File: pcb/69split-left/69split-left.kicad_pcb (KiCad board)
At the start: 2 copper layers, 157.1 x 105.3 mm, 89 parts, among them J1 Conn_02x03_Odd_Even, J2 USB_C_Receptacle, J3 USB_C_Receptacle_USB2.0_14P, SW1 SW_Push, SW10 Q, SW11 W, SW12 E, SW13 R, SW14 T, SW15 Caps Lock, SW16 A, SW17 S, SW18 D, SW19 F, SW2 Esc, SW20 G, SW21 Shift, SW22 \|, SW23 Z, SW24 X, SW25 C, SW26 V, SW27 B, SW28 Ctrl, SW29 Win, SW3 !,1,,F1, SW30 Alt, SW31 Space, SW4 @,2,,F2, SW5 #,3,,F3, SW6 $,4,,F4, SW7 %,5,,F5, SW8 ^,6,,F6, SW9 Tab, U1 ATmega32U4-AU, U2 TLV76133DCY, Y1 Crystal

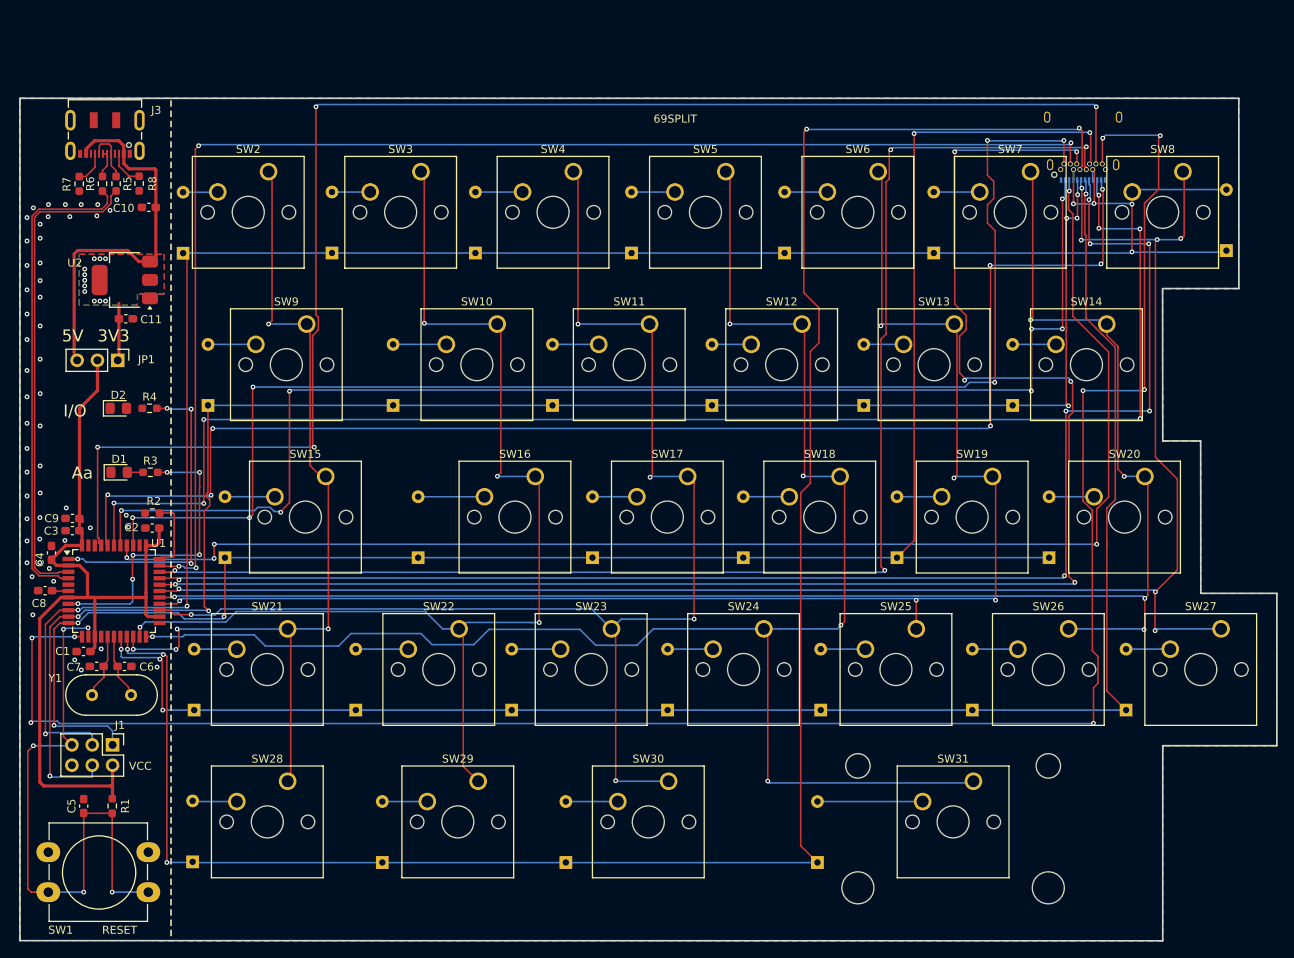
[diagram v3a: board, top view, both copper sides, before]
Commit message: Started changing things gain to use an I/O expander with I2C.
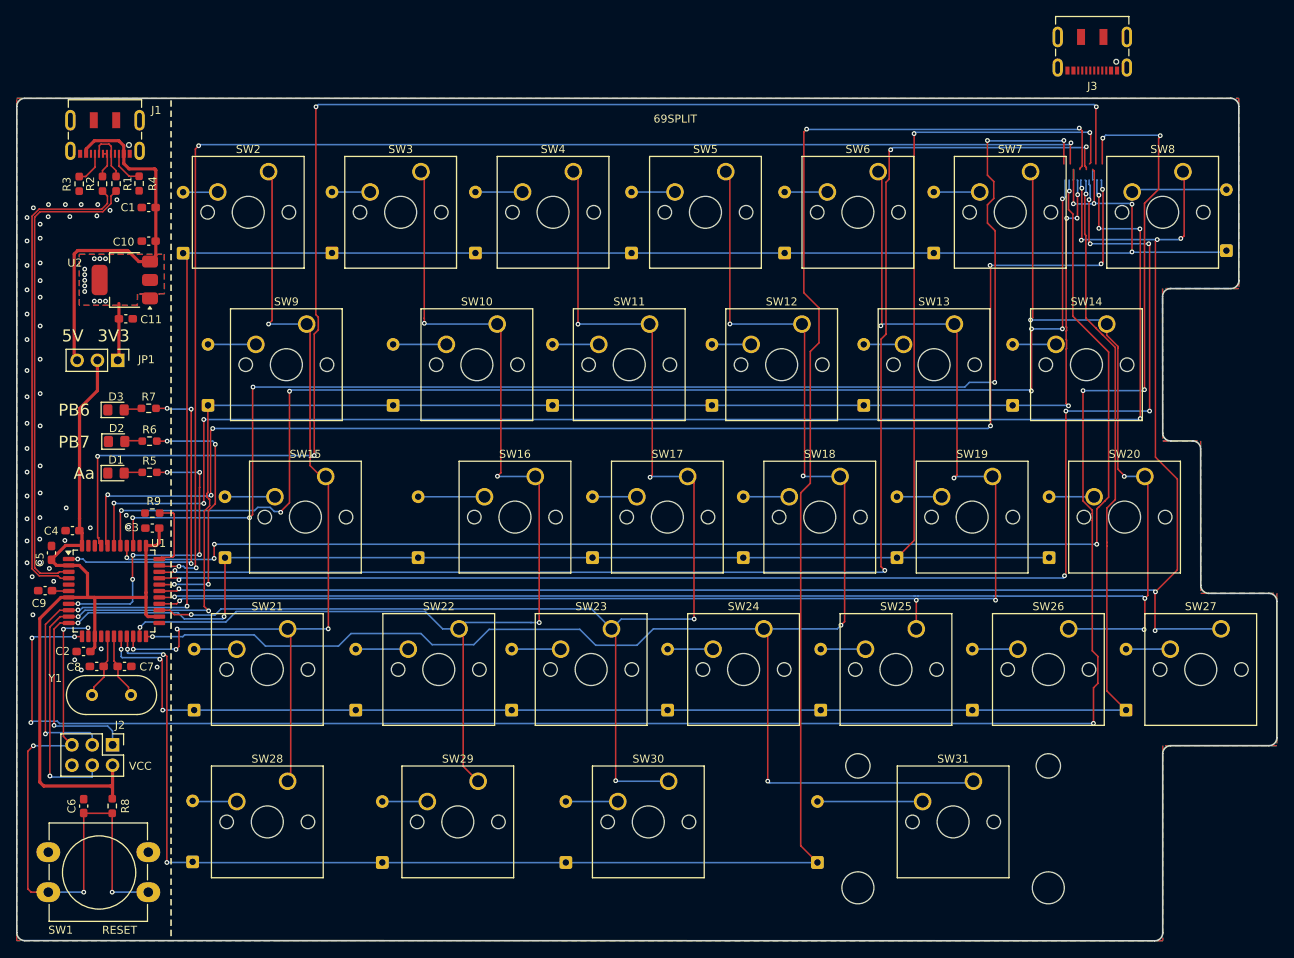
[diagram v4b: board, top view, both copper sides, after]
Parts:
- removed the J2 at (192.9, 43.0)
- added D3: Red LED, LED_SMD:LED_0805_2012Metric_Pad1.15x1.40mm_HandSolder, F.Cu at (72.0, 76.8)
- added J3: USB_C_Receptacle_USB2.0_16P, Connector_USB:USB_C_Receptacle_JAE_DX07S016JA1R1500, F.Cu at (194.0, 31.3)
- added R7: 200R, Resistor_SMD:R_0603_1608Metric_Pad0.98x0.95mm_HandSolder, F.Cu at (76.1, 76.6)
- J1: renamed from J3; value USB_C_Receptacle_USB2.0_14P -> USB_C_Receptacle_USB2.0_16P
- SW4: value @,2,,F2 -> ",2,,F2
- SW5: value #,3,,F3 -> £,3,,F3
- moved C1 40.0 mm to (76.1, 51.5)
- moved C10 4.22 mm to (76.1, 55.7)
- moved D2 4.16 mm to (72.1, 80.8)
- moved R6 4.10 mm to (76.2, 80.7)
- moved D1 0.40 mm to (72.0, 84.7)
- moved R5 0.11 mm to (76.2, 84.6)
- renumbered C9 to C1, C1 to C2, C2 to C3, C3 to C4, C4 to C5, C5 to C6, C6 to C7, C7 to C8, C8 to C9, D9 to D10, D10 to D11, D11 to D12, D12 to D13, D13 to D14, D14 to D15, D15 to D16, D16 to D17, D17 to D18, D18 to D19, D19 to D20, D20 to D21, D21 to D22, D22 to D23, D23 to D24, D24 to D25, D25 to D26, D26 to D27, D27 to D28, D28 to D29, D29 to D30, D30 to D31, D31 to D32, D32 to D33, D3 to D4, D4 to D5, D5 to D6, D6 to D7, D7 to D8, D8 to D9, J1 to J2, R5 to R1, R6 to R2, R7 to R3, R8 to R4, R3 to R5, R4 to R6, R1 to R8, R2 to R9
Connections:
- J1 pad A8: (no net) -> unconnected-(J1-SBU1-PadA8)
- J1 pad B8: (no net) -> unconnected-(J1-SBU2-PadB8)
- R6 pad 2: /ATmega32U4/INDICATOR_GPIO -> /ATmega32U4/INDICATOR_PB7
- U1 pad 1: /ATmega32U4/INDICATOR_GPIO -> /ATmega32U4/INDICATOR_CAPS_LOCK
- U1 pad 18: /ATmega32U4/ROW3 -> /ATmega32U4/SCL
- U1 pad 19: /ATmega32U4/ROW4 -> /ATmega32U4/SDA
- U1 pad 20: /ATmega32U4/COL0 -> /ATmega32U4/RX
- U1 pad 21: /ATmega32U4/COL1 -> /ATmega32U4/TX
- U1 pad 22: /ATmega32U4/COL3 -> /ATmega32U4/COL1
- U1 pad 25: /ATmega32U4/COL2 -> /ATmega32U4/COL0
- U1 pad 26: /ATmega32U4/COL4 -> /ATmega32U4/COL2
- U1 pad 27: /ATmega32U4/COL5 -> /ATmega32U4/COL3
- U1 pad 28: /ATmega32U4/COL6 -> /ATmega32U4/ROW3
- U1 pad 29: /ATmega32U4/GPIO_OUT_PB5 -> /ATmega32U4/ROW4
- U1 pad 31: /ATmega32U4/COL7 -> /ATmega32U4/INDICATOR_PB7
- U1 pad 32: /ATmega32U4/COL8 -> /ATmega32U4/INDICATOR_PB6
- U1 pad 36: /ATmega32U4/COL9 -> /ATmega32U4/COL5
- U1 pad 37: /ATmega32U4/COL10 -> /ATmega32U4/COL4
- U1 pad 38: /ATmega32U4/COL11 -> /ATmega32U4/ADC5
- U1 pad 39: /ATmega32U4/COL12 -> /ATmega32U4/ADC4
- U1 pad 40: /ATmega32U4/COL13 -> /ATmega32U4/ADC1
- U1 pad 41: /ATmega32U4/COL14 -> /ATmega32U4/ADC0
- U1 pad 8: /ATmega32U4/INDICATOR_CAPS_LOCK -> unconnected-(U1-PB0-Pad8)
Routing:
- net /ATmega32U4/INDICATOR_PB6: track 0.00 -> 208.8 mm, vias 0 -> 8
- net /ATmega32U4/INDICATOR_PB7: track 0.00 -> 203.4 mm, vias 0 -> 8
- net /ATmega32U4/GPIO_OUT_PB5: track 200.6 -> 0.00 mm, vias 6 -> 0
- net /ATmega32U4/COL14: track 187.6 -> 0.00 mm, vias 4 -> 0
- net /ATmega32U4/ADC0: track 0.00 -> 187.4 mm, vias 0 -> 4
- net /ATmega32U4/COL12: track 179.3 -> 0.00 mm, vias 7 -> 0
- net /ATmega32U4/ADC4: track 0.00 -> 179.3 mm, vias 0 -> 7
- net /ATmega32U4/COL4: track 177.5 -> 350.4 mm, vias 5 -> 10
- net /ATmega32U4/COL10: track 173.0 -> 0.00 mm, vias 5 -> 0
- net /ATmega32U4/COL7: track 171.9 -> 0.00 mm, vias 4 -> 0
- net /ATmega32U4/COL5: track 203.3 -> 374.8 mm, vias 5 -> 11
- net /ATmega32U4/COL9: track 171.4 -> 0.00 mm, vias 6 -> 0
- net /ATmega32U4/COL13: track 170.1 -> 0.00 mm, vias 7 -> 0
- net /ATmega32U4/ADC1: track 0.00 -> 170.1 mm, vias 0 -> 7
- net /ATmega32U4/COL8: track 169.6 -> 0.00 mm, vias 4 -> 0
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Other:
- board size 157.1 x 105.3 mm -> 157.5 x 105.3 mm
- board text added: "PB6"
- board text added: "PB7"
- board text removed: "I/O"

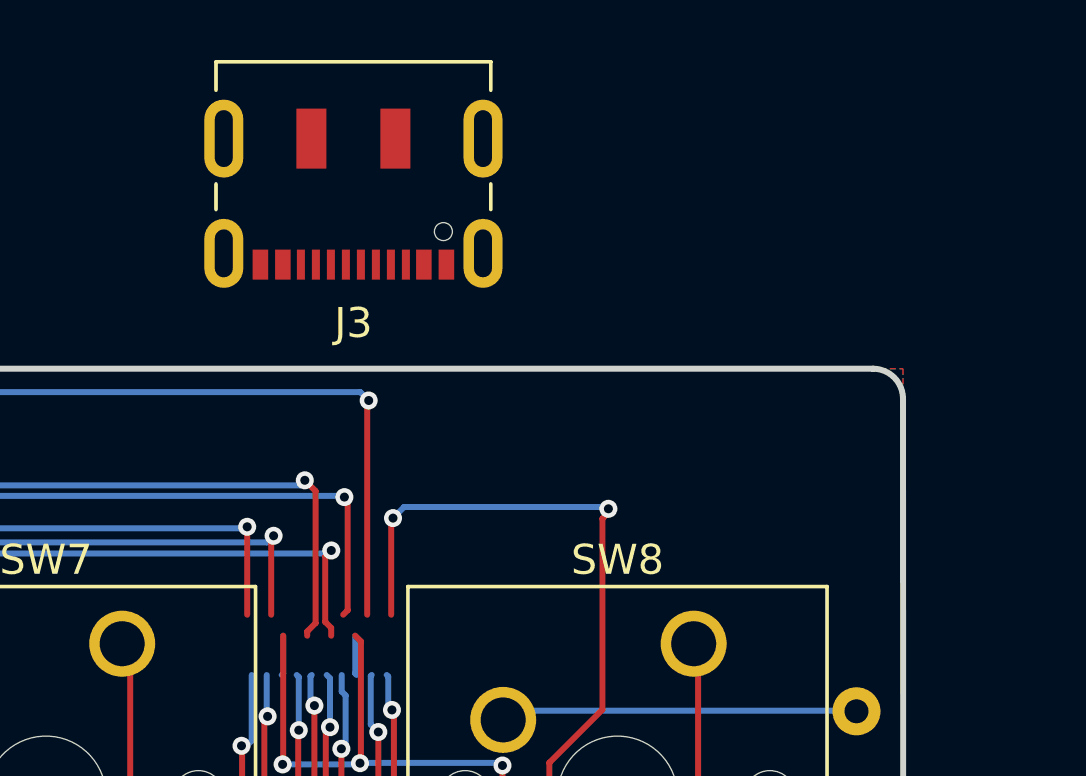
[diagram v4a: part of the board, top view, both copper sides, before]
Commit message: Continuing with I/O expander integration.
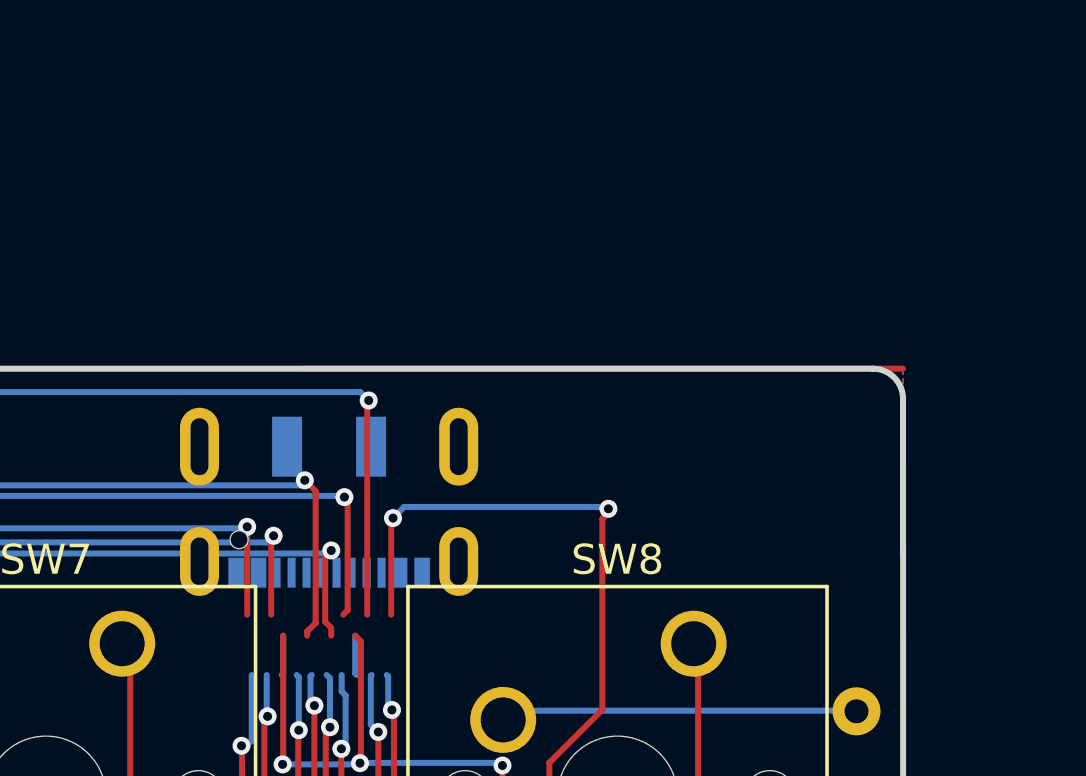
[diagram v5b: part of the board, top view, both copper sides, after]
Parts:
- J3: moved to B.Cu
- moved J3 10.3 mm to (193.2, 41.6), turned to 0 degrees

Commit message: Finished left keyboard again...
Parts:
- added R10: 1k, Resistor_SMD:R_0603_1608Metric_Pad0.98x0.95mm_HandSolder, F.Cu at (201.6, 41.6)
- added R11: 1k, Resistor_SMD:R_0603_1608Metric_Pad0.98x0.95mm_HandSolder, F.Cu at (201.6, 40.1)
- J3: moved to F.Cu
- moved J2 4.48 mm to (74.1, 115.0)
- moved R9 4.07 mm to (76.5, 85.6)
- moved SW1 3.69 mm to (63.5, 128.4)
- moved C10 3.69 mm to (76.1, 52.0)
- moved J1 3.69 mm to (70.6, 38.0)
- moved R1 3.69 mm to (72.0, 44.8)
- moved U2 3.69 mm to (73.1, 56.9)
- moved C1 3.69 mm to (76.1, 47.8)
- moved C11 3.69 mm to (73.2, 61.7)
- moved C3 3.69 mm to (76.5, 87.9)
- moved C4 3.69 mm to (66.6, 88.2)
- moved C5 3.69 mm to (63.9, 91.0)
- moved C6 3.69 mm to (68.0, 122.6)
- moved C9 3.69 mm to (63.1, 95.7)
- moved D1 3.69 mm to (72.0, 81.0)
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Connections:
- net /LDO & Jumper/3V3 renamed /3V3
- net /LDO & Jumper/USB_5V renamed /USB_5V
- U1 pad 36: /ATmega32U4/COL5 -> /ATmega32U4/COL6
- U1 pad 37: /ATmega32U4/COL4 -> /ATmega32U4/COL5
- U1 pad 38: /ATmega32U4/ADC5 -> /ATmega32U4/COL4
- U1 pad 8: unconnected-(U1-PB0-Pad8) -> /ATmega32U4/PB0/CS
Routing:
- net /ATmega32U4/SCL: track 0.00 -> 204.5 mm, vias 0 -> 4
- net /ATmega32U4/SDA: track 0.00 -> 203.5 mm, vias 0 -> 4
- net /ATmega32U4/ADC0: track 187.4 -> 0.00 mm, vias 4 -> 0
- net /ATmega32U4/INDICATOR_PB6: track 208.8 -> 23.2 mm, vias 8 -> 0
- net VCC: track 107.4 -> 291.0 mm, vias 0 -> 10
- net /ATmega32U4/ADC4: track 179.3 -> 0.00 mm, vias 7 -> 0
- net /ATmega32U4/INDICATOR_PB7: track 203.4 -> 25.8 mm, vias 8 -> 4
- net /ATmega32U4/ADC1: track 170.1 -> 0.00 mm, vias 7 -> 0
- net /ATmega32U4/ADC5: track 163.7 -> 0.00 mm, vias 7 -> 0
- net /ATmega32U4/COL5: track 374.8 -> 220.6 mm, vias 11 -> 7
- net /ATmega32U4/COL4: track 350.4 -> 199.0 mm, vias 10 -> 7
- net /ATmega32U4/ROW4: track 248.4 -> 119.7 mm, vias 5 -> 0
- net /ATmega32U4/ROW2: track 234.4 -> 153.1 mm, vias 5 -> 3
- net /ATmega32U4/ROW3: track 204.0 -> 142.8 mm, vias 4 -> 2
- net /ATmega32U4/ROW1: track 210.0 -> 171.8 mm, vias 7 -> 3
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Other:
- board size 157.5 x 105.3 mm -> 157.5 x 108.9 mm
- board text added: "2RIGHT"

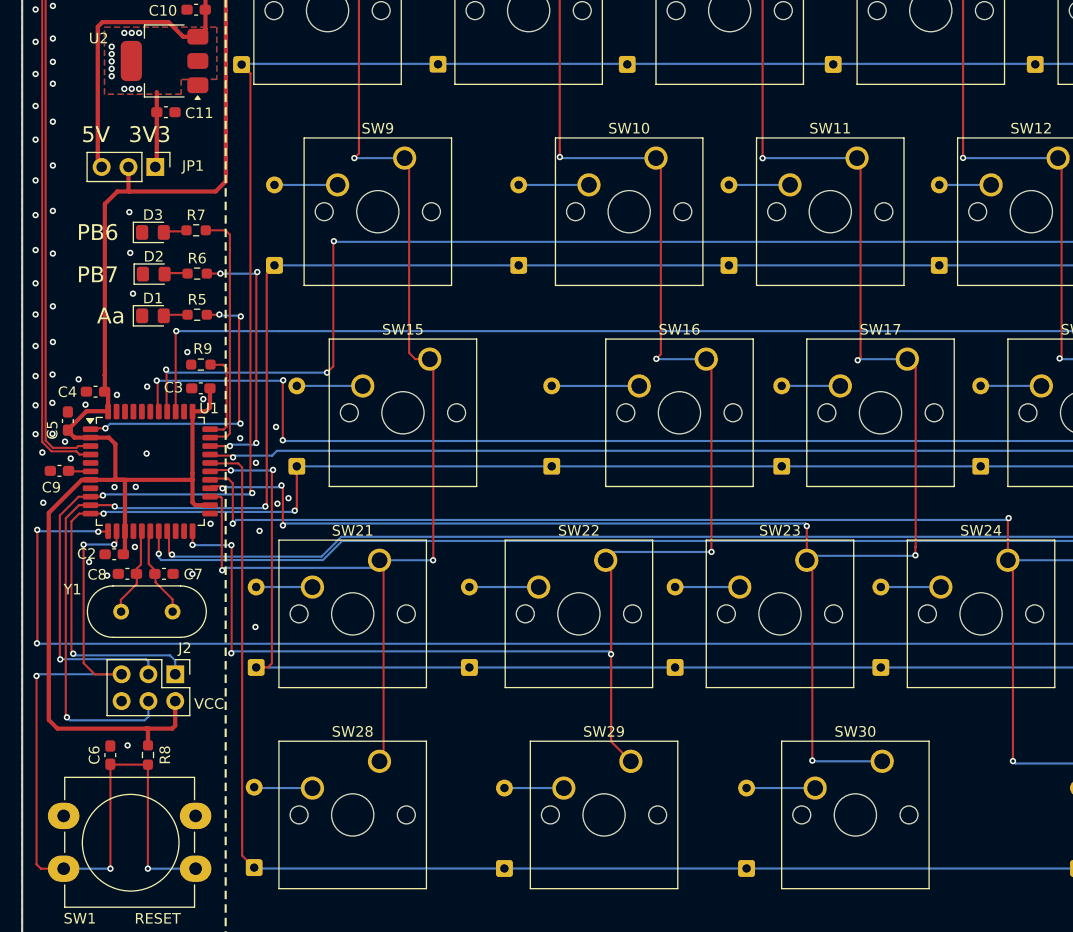
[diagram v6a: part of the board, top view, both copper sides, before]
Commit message: Minor improvements to left schematic and layout.
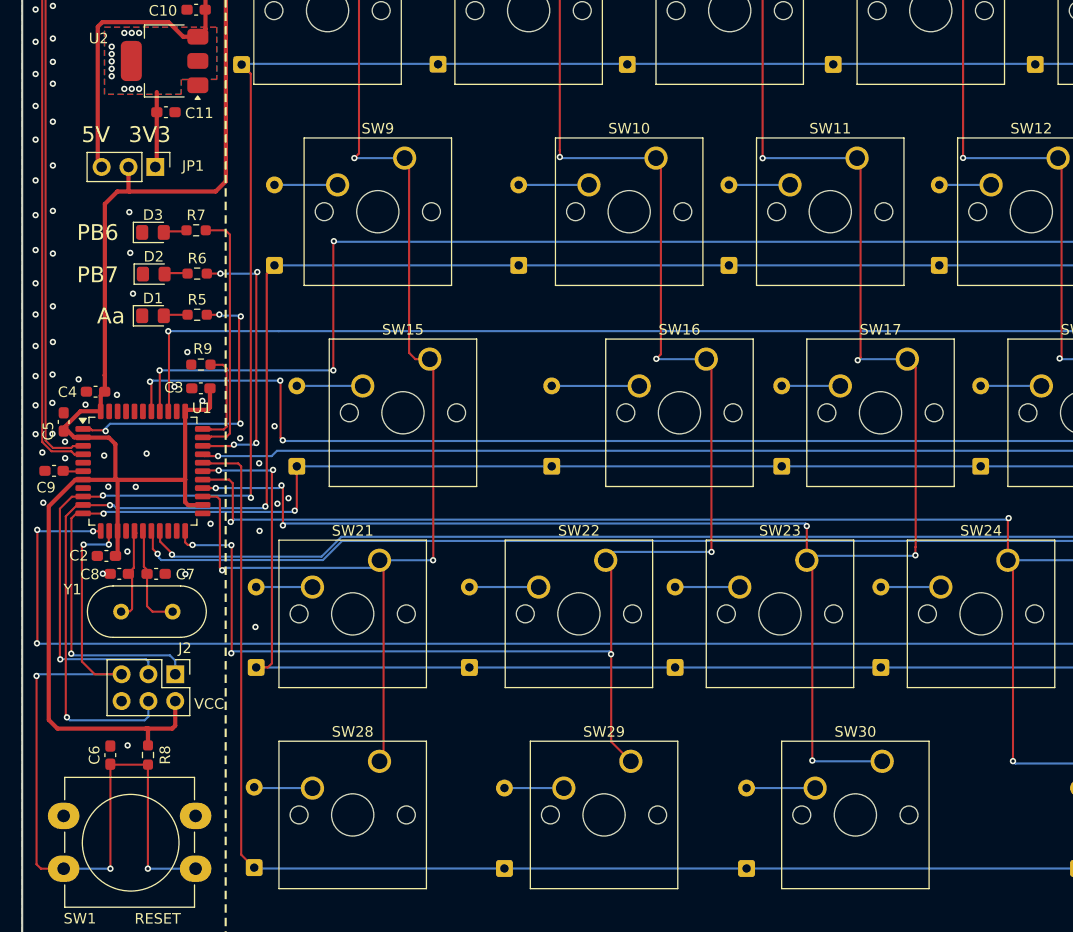
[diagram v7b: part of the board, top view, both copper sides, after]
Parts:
- SW10: value Q -> SW_Push
- SW11: value W -> SW_Push
- SW12: value E -> SW_Push
- SW13: value R -> SW_Push
- SW14: value T -> SW_Push
- SW15: value Caps Lock -> SW_Push
- SW16: value A -> SW_Push
- SW17: value S -> SW_Push
- SW18: value D -> SW_Push
- SW19: value F -> SW_Push
- SW2: value Esc -> SW_Push
- SW20: value G -> SW_Push
- SW21: value Shift -> SW_Push
- SW22: value \| -> SW_Push
- SW23: value Z -> SW_Push
- SW24: value X -> SW_Push
- SW25: value C -> SW_Push
- SW26: value V -> SW_Push
- SW27: value B -> SW_Push
- SW28: value Ctrl -> SW_Push
- SW29: value Win -> SW_Push
- SW3: value !,1,,F1 -> SW_Push
- SW30: value Alt -> SW_Push
- SW31: value Space -> SW_Push
- SW4: value ",2,,F2 -> SW_Push
- SW5: value £,3,,F3 -> SW_Push
- SW6: value $,4,,F4 -> SW_Push
- SW7: value %,5,,F5 -> SW_Push
- SW8: value ^,6,,F6 -> SW_Push
- SW9: value Tab -> SW_Push
- moved C8 0.77 mm to (68.8, 105.5)
- moved C2 0.76 mm to (67.6, 103.8)
- moved C7 0.75 mm to (72.3, 105.5)
- moved U1 0.70 mm to (71.0, 95.7)
- moved C9 0.51 mm to (62.6, 95.7)
- moved C5 0.41 mm to (63.5, 91.1)
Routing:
- net /ATmega32U4/INDICATOR_PB7: track 25.8 -> 27.4 mm
- net Net-(U1-XTAL1): track 8.59 -> 10.1 mm
- net /ATmega32U4/INDICATOR_CAPS_LOCK: track 28.0 -> 29.1 mm
- net Net-(U1-XTAL2): track 8.46 -> 9.28 mm
- net /ATmega32U4/ROW0: track 214.6 -> 215.4 mm
- net /ATmega32U4/COL3: track 210.1 -> 210.8 mm
- net /ATmega32U4/GPIO_OUT_PB7: track 249.3 -> 248.6 mm
- net /ATmega32U4/COL6: track 204.8 -> 205.6 mm
- net /ATmega32U4/ROW4: track 119.7 -> 120.4 mm
- net /ATmega32U4/INDICATOR_PB6: track 23.2 -> 23.9 mm
- net /ATmega32U4/COL5: track 220.6 -> 221.3 mm
- net /ATmega32U4/D-: track 60.5 -> 59.8 mm
- net /ATmega32U4/D+: track 61.0 -> 60.3 mm
- net /ATmega32U4/GPIO_OUT_PB6: track 173.5 -> 174.1 mm
- net Net-(U1-UCAP): track 2.28 -> 2.88 mm
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
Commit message: Alright I think now the left side is actually ready.
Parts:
- added J4: Conn_01x09_Socket, Connector_PinHeader_2.54mm:PinHeader_1x11_P2.54mm_Vertical, F.Cu at (81.5, 36.2)
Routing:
- net /ATmega32U4/PB0/CS: track 0.00 -> 149.3 mm, vias 0 -> 2
- net /ATmega32U4/RX: track 0.00 -> 84.7 mm, vias 0 -> 2
- net /ATmega32U4/TX: track 0.00 -> 80.7 mm, vias 0 -> 2
- net /ATmega32U4/ADC4: track 0.00 -> 80.5 mm, vias 0 -> 2
- net /ATmega32U4/ADC1: track 0.00 -> 80.5 mm, vias 0 -> 2
- net /ATmega32U4/ADC0: track 0.00 -> 77.3 mm, vias 0 -> 2
- net /ATmega32U4/SCL: track 204.8 -> 280.2 mm, vias 4 -> 5
- net /ATmega32U4/SDA: track 204.0 -> 271.5 mm, vias 4 -> 5
- net /3V3: track 7.16 -> 30.6 mm
- net /USB_5V: track 48.0 -> 58.7 mm
- net /ATmega32U4/COL0: track 112.5 -> 111.6 mm
- net /ATmega32U4/COL6: track 205.6 -> 204.8 mm
- net GND: vias 68 -> 98
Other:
- board text added: "GND"
- board text added: "PB0/CS"
- board text added: "PF0/ADC0"
- board text added: "PF1/ADC1"
- board text added: "PF4/ADC4"
- board text added: "RX"
- board text added: "SCL"
- board text added: "SDA"
- board text added: "TX"
- board text added: "USB5V"
